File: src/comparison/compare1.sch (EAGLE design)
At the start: 8 parts, among them Q1 BSS92, Q2 BSS92, Q3 BSS97, Q4 BSS97, Q5 BSS92

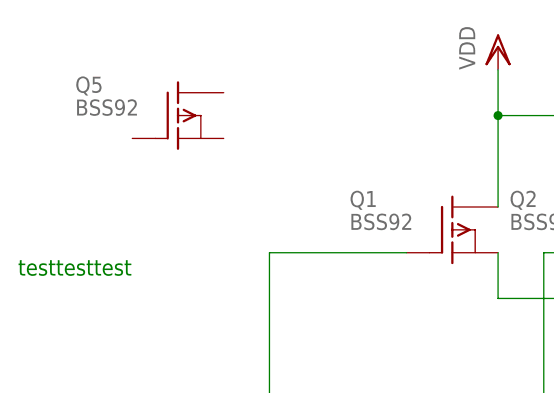
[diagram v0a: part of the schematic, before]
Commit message: added a simple test class for emf compare
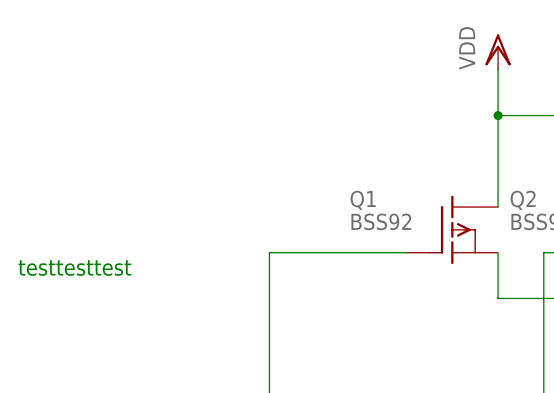
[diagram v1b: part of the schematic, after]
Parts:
- removed Q5: BSS92, transistor-fet:BSS92
- Q1: UID (none) -> 8
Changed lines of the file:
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@@
 <attribute name="P1" value="0001"/>
 <attribute name="TEST2" value="5"/>
+<attribute name="UID" value="8"/>
 </part>
 <part name="Q2" library="transistor-fet" deviceset="BSS92" device="">
@@
 <part name="A" library="pinhead" deviceset="PINHD-1X1" device=""/>
 <part name="B" library="pinhead" deviceset="PINHD-1X1" device=""/>
-<part name="Q5" library="transistor-fet" deviceset="BSS92" device="">
-<attribute name="P1" value="0001"/>
-<attribute name="TEST2" value="5"/>
-</part>
 </parts>
 <sheets>
@@
 <attribute name="P1" x="-182.88" y="172.72" size="1.778" layer="96" display="off"/>
 <attribute name="TEST2" x="-182.88" y="172.72" size="1.778" layer="96" display="off"/>
+<attribute name="UID" x="-182.88" y="172.72" size="1.778" layer="96" display="off"/>
 </instance>
 <instance part="Q2" gate="G$1" x="-165.1" y="172.72">
@@
 <instance part="A" gate="G$1" x="-215.9" y="137.16" rot="R180"/>
 <instance part="B" gate="G$1" x="-215.9" y="119.38" rot="R180"/>
-<instance part="Q5" gate="G$1" x="-213.36" y="185.42">
-<attribute name="P1" x="-213.36" y="185.42" size="1.778" layer="96" display="off"/>
-<attribute name="TEST2" x="-213.36" y="185.42" size="1.778" layer="96" display="off"/>
-</instance>
 </instances>
 <busses>
